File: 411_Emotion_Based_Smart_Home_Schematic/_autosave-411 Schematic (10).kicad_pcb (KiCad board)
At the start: 2 copper layers, 123 x 48 mm, 25 parts, among them Q1 NSS1C301ET4G, Q2 NSS1C301ET4G, Q3 NSS1C301ET4G, U4 HC-SR04

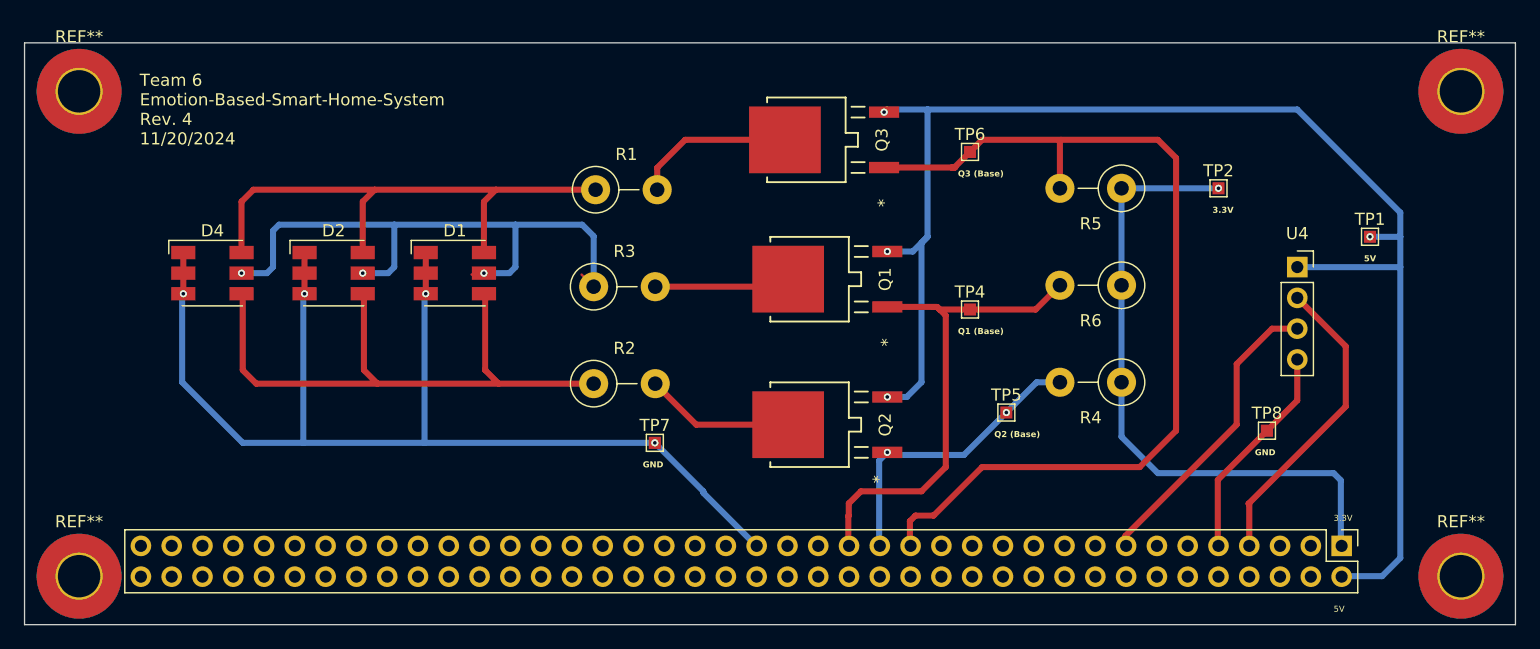
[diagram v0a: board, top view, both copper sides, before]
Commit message: Updated schematic.
Added limiting resistors to each GPIO pins.
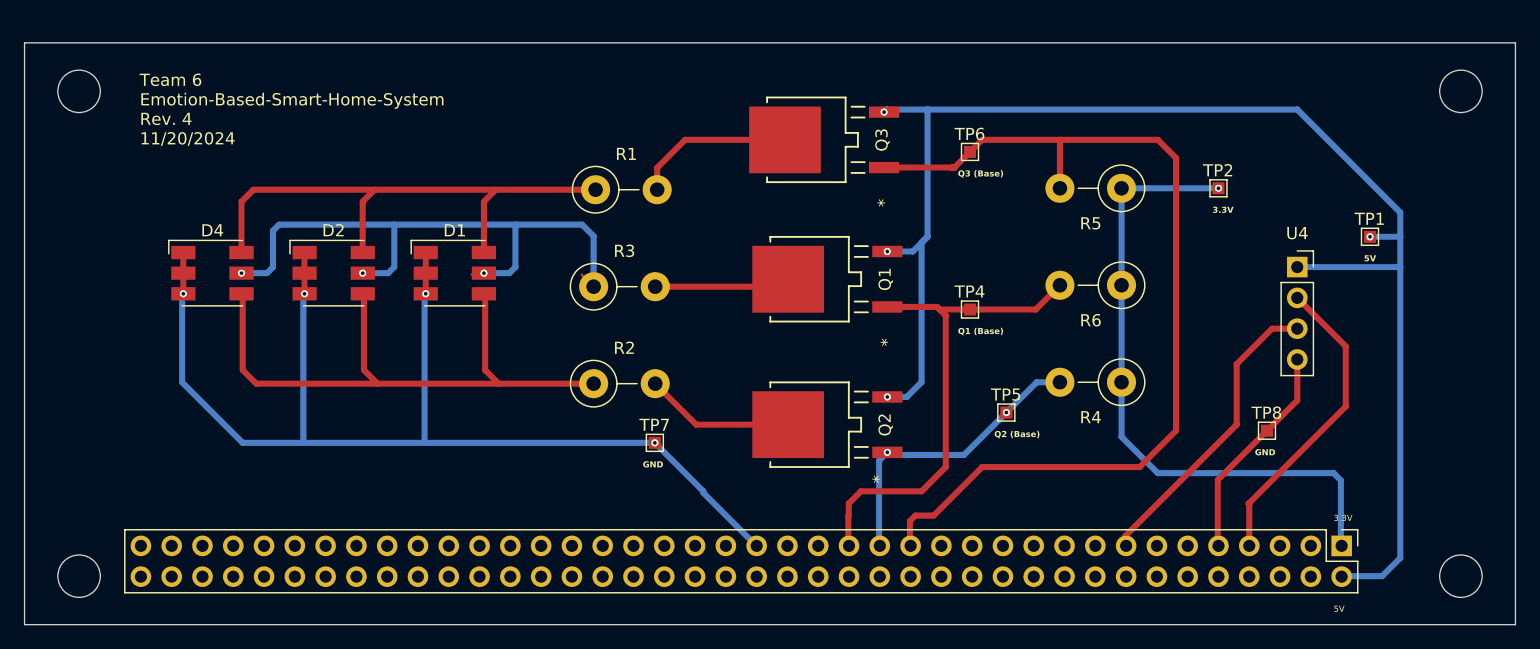
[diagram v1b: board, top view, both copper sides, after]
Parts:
- removed REF** (x4): MountingHole_3.5mm_Pad_TopBottom, MountingHole:MountingHole_3.5mm_Pad_TopBottom
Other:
- outline, holes or cut-outs redrawn
